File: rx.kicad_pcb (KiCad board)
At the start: 2 copper layers, 100 x 80 mm, 137 parts, among them J1 RX-RF, J10 ROT, J11 TxOsc, J13 Conn_Coaxial, J2 HP, J3 AVR-ISP-6, J4 ToPA, J5 Key, J6 Supply, J7 SW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

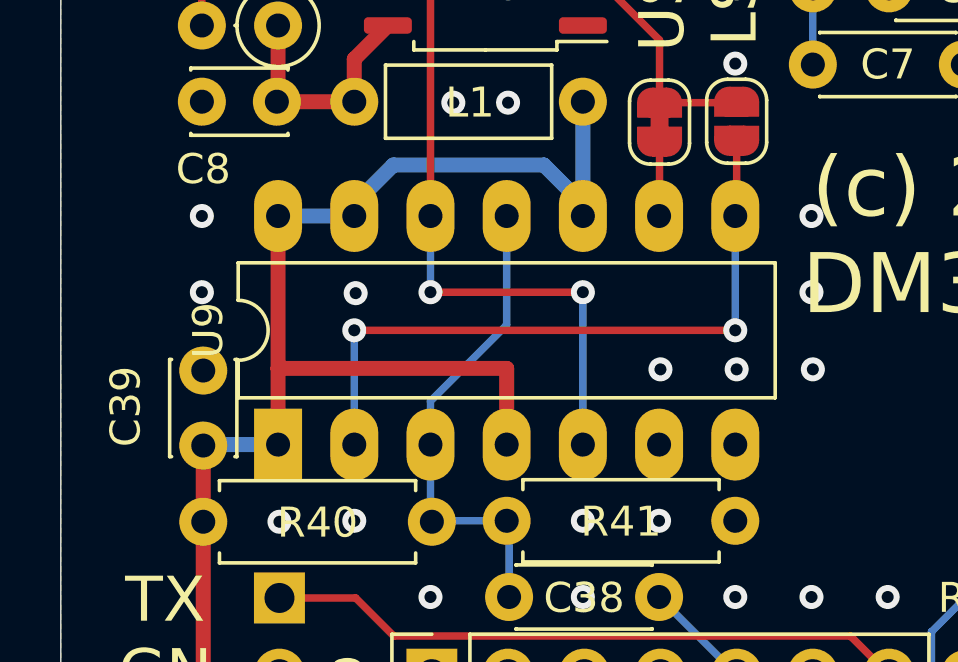
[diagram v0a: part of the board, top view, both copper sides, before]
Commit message: Added missing sub-circuits.
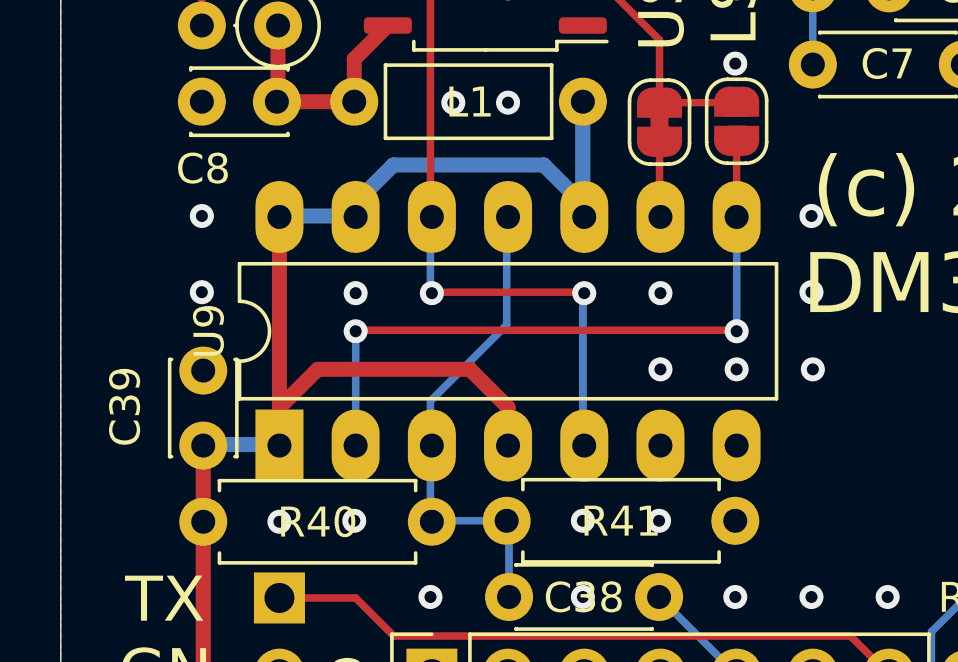
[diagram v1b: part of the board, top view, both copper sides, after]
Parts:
- moved U9 0.06 mm to (110.8, 106.0)
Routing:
- net +5VD: track 242.8 -> 244.2 mm
- net GND: vias 139 -> 140
